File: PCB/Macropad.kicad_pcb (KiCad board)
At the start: 2 copper layers, 44 x 61.3 mm, 9 parts, among them SW1 SW_Push, SW2 SW_Push, SW3 SW_Push, SW4 SW_Push, U1 XIAO-RP2040-DIP

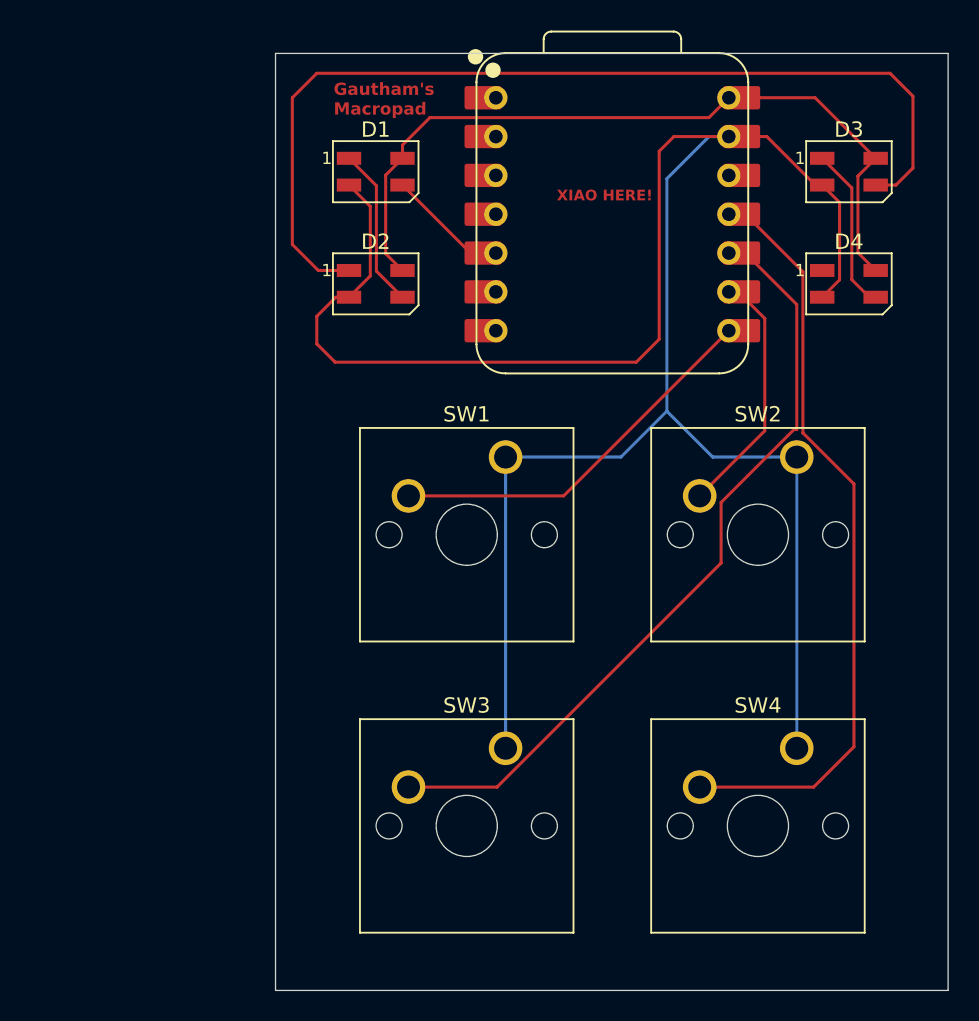
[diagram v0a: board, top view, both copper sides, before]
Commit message: Added OLED
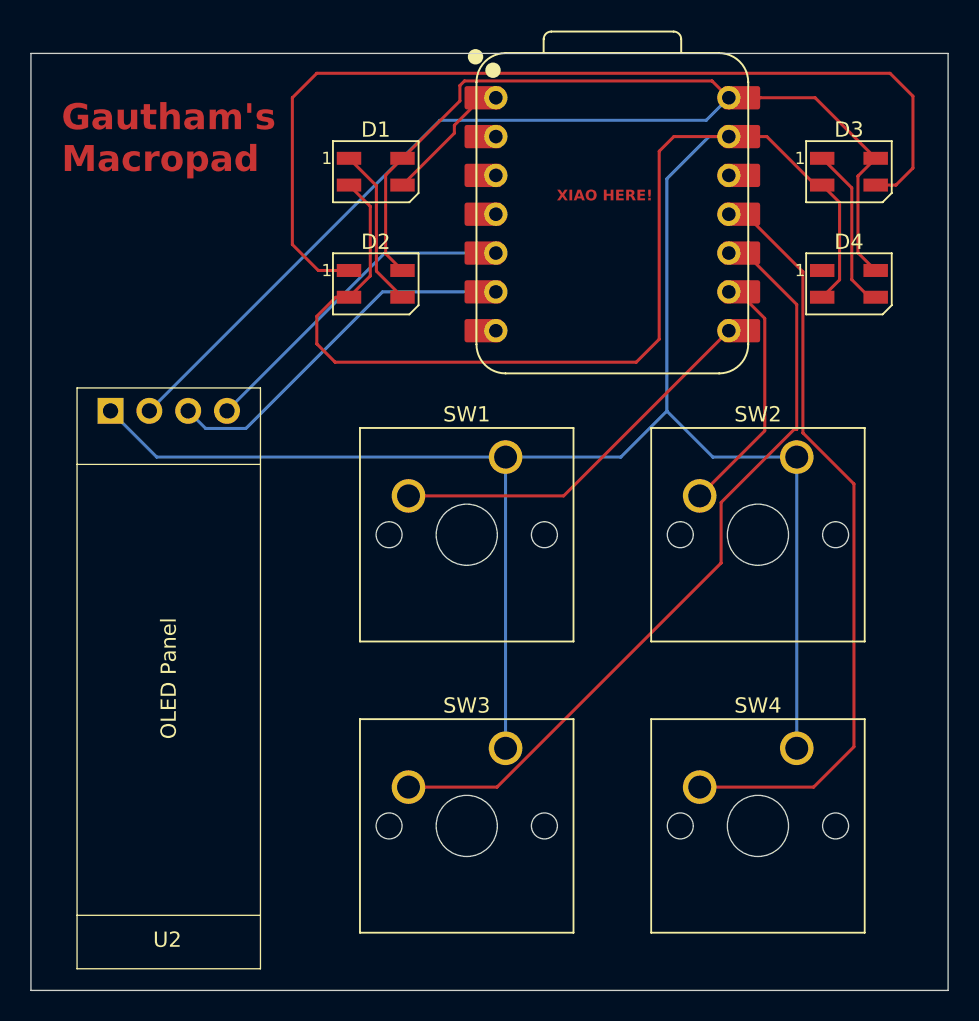
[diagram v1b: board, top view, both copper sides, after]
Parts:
- added U2: ~, OLED:SSD1306-0.91-OLED-4pin-128x32, F.Cu at (94.6, 118.9)
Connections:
- U1 pad 1: unconnected-(U1-GPIO26/ADC0/A0-Pad1) -> Net-(D1-DIN)
- U1 pad 5: Net-(D1-DIN) -> SDA
- U1 pad 6: unconnected-(U1-GPIO7/SCL-Pad6) -> SCL
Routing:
- net +5V: track 51.7 -> 99.1 mm
- net GND: track 148.6 -> 175.7 mm
- net SCL: track 0.00 -> 24.3 mm
- net SDA: track 0.00 -> 23.5 mm
- net Net-(D1-DIN): track 7.95 -> 8.78 mm
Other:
- board size 44 x 61.3 mm -> 60 x 61.3 mm
